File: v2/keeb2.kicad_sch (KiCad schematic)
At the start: 24 parts, among them J1 AVR-ISP-6, J3 AudioJack4, SW2 SW_Push_Reset, SW71 RotaryEncoder_Switch, U1 ATmega32U4-A, Y1 XTAL

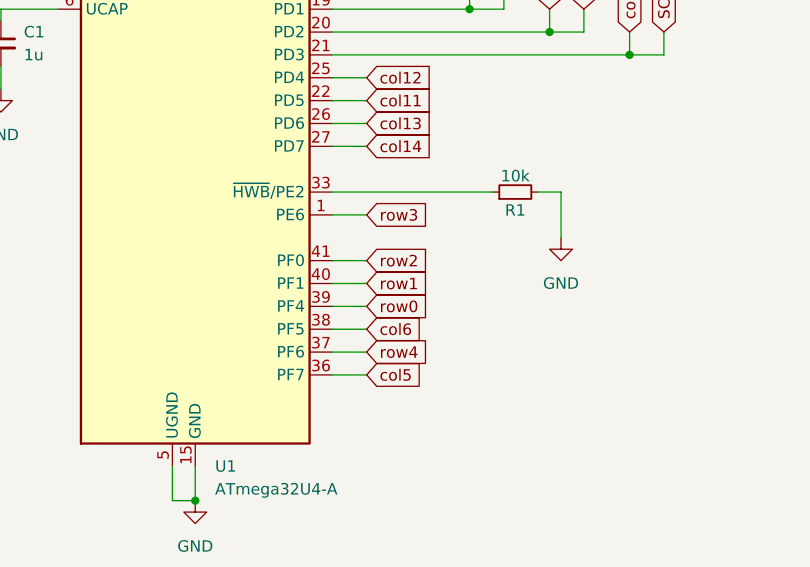
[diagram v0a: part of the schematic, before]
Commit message: Linked part of the design; need to move reset button &  ISP
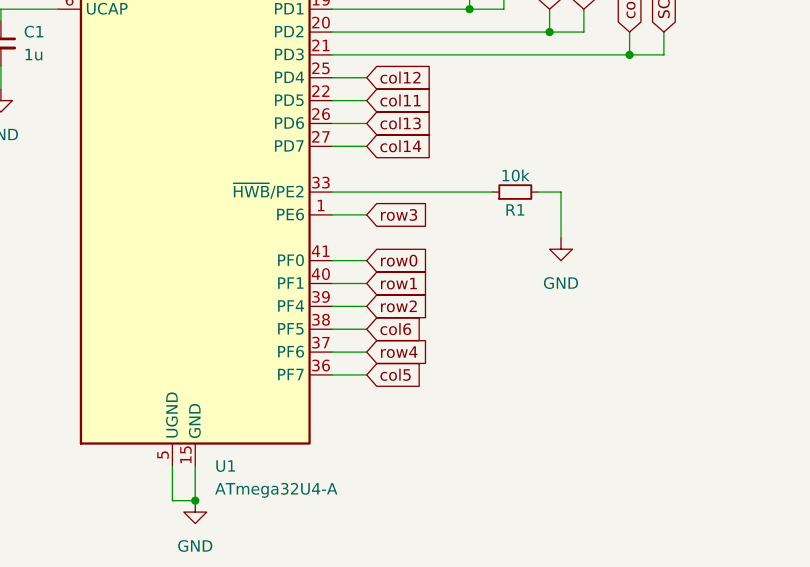
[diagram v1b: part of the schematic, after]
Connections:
- net row0: now also U1.41 (PF0); no longer U1.39 (PF4)
- net row2: now also U1.39 (PF4); no longer U1.41 (PF0)

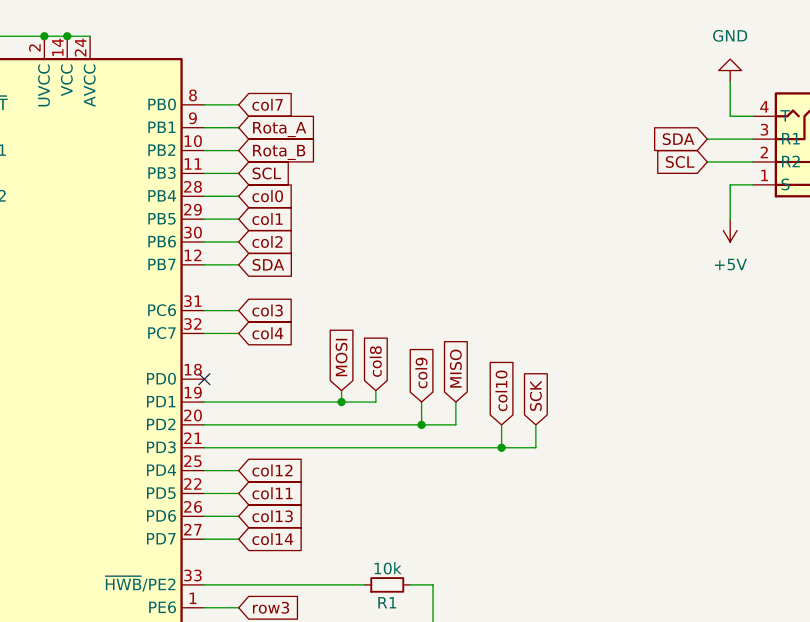
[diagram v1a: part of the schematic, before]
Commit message: Moved ISP and reset button. Finished routing
Moved the ISP IO to make it easier to route them to the MCU
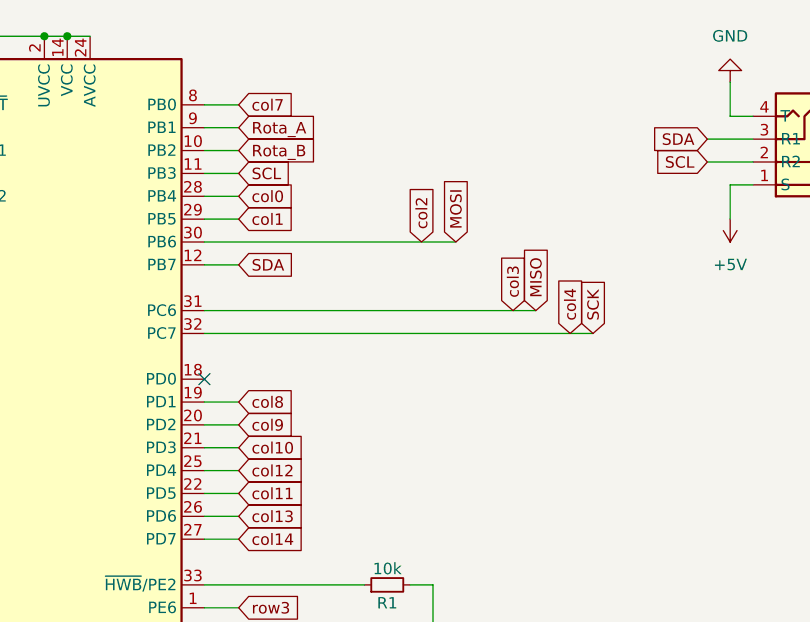
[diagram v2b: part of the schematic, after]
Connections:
- net col2 is gone; now on net MOSI: U1.30 (PB6)
- net col3 is gone; now on net MISO: U1.31 (PC6)
- net col4 is gone; now on net SCK: U1.32 (PC7)
- net MISO: no longer U1.20 (PD2)
- net MOSI: no longer U1.19 (PD1)
- net SCK: no longer U1.21 (PD3)
- new net col10: U1.21 (PD3)
- new net col8: U1.19 (PD1)
- new net col9: U1.20 (PD2)
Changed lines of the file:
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@@
-	)
-	(junction
-		(at 243.84 85.09)
-		(diameter 0)
-		(color 0 0 0 0)
-	)
-	(junction
-		(at 234.95 82.55)
-		(diameter 0)
-		(color 0 0 0 0)
 	)
 	(junction
@@
 	)
 	(junction
-		(at 226.06 80.01)
-		(diameter 0)
-		(color 0 0 0 0)
-	)
-	(junction
 		(at 66.04 93.98)
 		(diameter 0)
@@
 	(wire
 		(pts
-			(xy 210.82 72.39) (xy 214.63 72.39)
+			(xy 210.82 72.39) (xy 254 72.39)
 		)
 		(stroke
@@
 	(wire
 		(pts
-			(xy 234.95 82.55) (xy 238.76 82.55)
-		)
-		(stroke
-			(width 0)
-			(type default)
-		)
-	)
-	(wire
-		(pts
 			(xy 128.27 52.07) (xy 134.62 52.07)
 		)
@@
 	(wire
 		(pts
-			(xy 210.82 80.01) (xy 226.06 80.01)
-		)
-		(stroke
-			(width 0)
-			(type default)
-		)
-	)
-	(wire
-		(pts
 			(xy 173.99 80.01) (xy 173.99 81.28)
 		)
@@
 	(wire
 		(pts
-			(xy 243.84 85.09) (xy 247.65 85.09)
-		)
-		(stroke
-			(width 0)
-			(type default)
-		)
-	)
-	(wire
-		(pts
 			(xy 210.82 115.57) (xy 214.63 115.57)
 		)
@@
 	(wire
 		(pts
-			(xy 210.82 62.23) (xy 214.63 62.23)
-		)
-		(stroke
-			(width 0)
-			(type default)
-		)
-	)
-	(wire
-		(pts
-			(xy 247.65 82.55) (xy 247.65 85.09)
+			(xy 210.82 62.23) (xy 238.76 62.23)
 		)
 		(stroke
@@
 	(wire
 		(pts
+			(xy 210.82 85.09) (xy 214.63 85.09)
+		)
+		(stroke
+			(width 0)
+			(type default)
+		)
+	)
+	(wire
+		(pts
 			(xy 210.82 54.61) (xy 214.63 54.61)
 		)
@@
 	(wire
 		(pts
-			(xy 210.82 85.09) (xy 243.84 85.09)
-		)
-		(stroke
-			(width 0)
-			(type default)
-		)
-	)
-	(wire
-		(pts
 			(xy 50.8 33.02) (xy 50.8 38.1)
 		)
@@
 	(wire
 		(pts
-			(xy 210.82 82.55) (xy 234.95 82.55)
-		)
-		(stroke
-			(width 0)
-			(type default)
-		)
-	)
-	(wire
-		(pts
 			(xy 210.82 46.99) (xy 214.63 46.99)
 		)
@@
 	(wire
 		(pts
-			(xy 226.06 80.01) (xy 229.87 80.01)
-		)
-		(stroke
-			(width 0)
-			(type default)
-		)
-	)
-	(wire
-		(pts
 			(xy 210.82 90.17) (xy 214.63 90.17)
 		)
@@
 	(wire
 		(pts
+			(xy 210.82 80.01) (xy 214.63 80.01)
+		)
+		(stroke
+			(width 0)
+			(type default)
+		)
+	)
+	(wire
+		(pts
 			(xy 45.72 78.74) (xy 45.72 83.82)
 		)
@@
 	(wire
 		(pts
+			(xy 210.82 82.55) (xy 214.63 82.55)
+		)
+		(stroke
+			(width 0)
+			(type default)
+		)
+	)
+	(wire
+		(pts
 			(xy 39.37 76.2) (xy 46.99 76.2)
 		)
@@
 	(wire
 		(pts
-			(xy 210.82 69.85) (xy 214.63 69.85)
+			(xy 210.82 69.85) (xy 247.65 69.85)
 		)
 		(stroke
@@
 	(wire
 		(pts
-			(xy 234.95 82.55) (xy 234.95 80.01)
-		)
-		(stroke
-			(width 0)
-			(type default)
-		)
-	)
-	(wire
-		(pts
 			(xy 62.23 83.82) (xy 63.5 83.82)
 		)
@@
 	(wire
 		(pts
-			(xy 226.06 80.01) (xy 226.06 78.74)
-		)
-		(stroke
-			(width 0)
-			(type default)
-		)
-	)
-	(wire
-		(pts
 			(xy 269.24 55.88) (xy 269.24 59.69)
 		)
@@
 	(wire
 		(pts
-			(xy 238.76 80.01) (xy 238.76 82.55)
-		)
-		(stroke
-			(width 0)
-			(type default)
-		)
-	)
-	(wire
-		(pts
 			(xy 123.19 157.48) (xy 128.27 157.48)
 		)
@@
 	(wire
 		(pts
-			(xy 229.87 78.74) (xy 229.87 80.01)
-		)
-		(stroke
-			(width 0)
-			(type default)
-		)
-	)
-	(wire
-		(pts
 			(xy 39.37 33.02) (xy 39.37 38.1)
 		)
@@
 		(pts
 			(xy 62.23 27.94) (xy 62.23 22.86)
-		)
-		(stroke
-			(width 0)
-			(type default)
-		)
-	)
-	(wire
-		(pts
-			(xy 243.84 85.09) (xy 243.84 82.55)
 		)
 		(stroke
@@
 	(global_label "col2"
 		(shape input)
-		(at 214.63 62.23 0)
-		(fields_autoplaced yes)
-		(effects
-			(font
-				(size 1.27 1.27)
-			)
-			(justify left)
-		)
-		(property "Intersheetrefs" "${INTERSHEET_REFS}"
-			(at 221.7275 62.23 0)
+		(at 234.95 62.23 90)
+		(fields_autoplaced yes)
+		(effects
+			(font
+				(size 1.27 1.27)
+			)
+			(justify left)
+		)
+		(property "Intersheetrefs" "${INTERSHEET_REFS}"
+			(at 234.95 55.1325 90)
 			(effects
 				(font
@@
 	(global_label "col9"
 		(shape input)
-		(at 234.95 80.01 90)
-		(fields_autoplaced yes)
-		(effects
-			(font
-				(size 1.27 1.27)
-			)
-			(justify left)
-		)
-		(property "Intersheetrefs" "${INTERSHEET_REFS}"
-			(at 234.95 72.9125 90)
+		(at 214.63 82.55 0)
+		(fields_autoplaced yes)
+		(effects
+			(font
+				(size 1.27 1.27)
+			)
+			(justify left)
+		)
+		(property "Intersheetrefs" "${INTERSHEET_REFS}"
+			(at 221.7275 82.55 0)
 			(effects
 				(font
@@
 	(global_label "MISO"
 		(shape input)
-		(at 238.76 80.01 90)
-		(fields_autoplaced yes)
-		(effects
-			(font
-				(size 1.27 1.27)
-			)
-			(justify left)
-		)
-		(property "Intersheetrefs" "${INTERSHEET_REFS}"
-			(at 238.76 72.4286 90)
+		(at 247.65 69.85 90)
+		(fields_autoplaced yes)
+		(effects
+			(font
+				(size 1.27 1.27)
+			)
+			(justify left)
+		)
+		(property "Intersheetrefs" "${INTERSHEET_REFS}"
+			(at 247.65 62.2686 90)
 			(effects
 				(font
@@
 	(global_label "MOSI"
 		(shape input)
-		(at 226.06 78.74 90)
-		(fields_autoplaced yes)
-		(effects
-			(font
-				(size 1.27 1.27)
-			)
-			(justify left)
-		)
-		(property "Intersheetrefs" "${INTERSHEET_REFS}"
-			(at 226.06 71.1586 90)
+		(at 238.76 62.23 90)
+		(fields_autoplaced yes)
+		(effects
+			(font
+				(size 1.27 1.27)
+			)
+			(justify left)
+		)
+		(property "Intersheetrefs" "${INTERSHEET_REFS}"
+			(at 238.76 54.6486 90)
 			(effects
 				(font
@@
 	(global_label "SCK"
 		(shape input)
-		(at 247.65 82.55 90)
-		(fields_autoplaced yes)
-		(effects
-			(font
-				(size 1.27 1.27)
-			)
-			(justify left)
-		)
-		(property "Intersheetrefs" "${INTERSHEET_REFS}"
-			(at 247.65 75.8153 90)
+		(at 254 72.39 90)
+		(fields_autoplaced yes)
+		(effects
+			(font
+				(size 1.27 1.27)
+			)
+			(justify left)
+		)
+		(property "Intersheetrefs" "${INTERSHEET_REFS}"
+			(at 254 65.6553 90)
 			(effects
 				(font
@@
 	(global_label "col3"
 		(shape input)
-		(at 214.63 69.85 0)
-		(fields_autoplaced yes)
-		(effects
-			(font
-				(size 1.27 1.27)
-			)
-			(justify left)
-		)
-		(property "Intersheetrefs" "${INTERSHEET_REFS}"
-			(at 221.7275 69.85 0)
+		(at 245.11 69.85 90)
+		(fields_autoplaced yes)
+		(effects
+			(font
+				(size 1.27 1.27)
+			)
+			(justify left)
+		)
+		(property "Intersheetrefs" "${INTERSHEET_REFS}"
+			(at 245.11 62.7525 90)
 			(effects
 				(font
@@
 	(global_label "col10"
 		(shape input)
-		(at 243.84 82.55 90)
-		(fields_autoplaced yes)
-		(effects
-			(font
-				(size 1.27 1.27)
-			)
-			(justify left)
-		)
-		(property "Intersheetrefs" "${INTERSHEET_REFS}"
-			(at 243.84 74.243 90)
+		(at 214.63 85.09 0)
+		(fields_autoplaced yes)
+		(effects
+			(font
+				(size 1.27 1.27)
+			)
+			(justify left)
+		)
+		(property "Intersheetrefs" "${INTERSHEET_REFS}"
+			(at 222.937 85.09 0)
 			(effects
 				(font
@@
 	(global_label "col4"
 		(shape input)
-		(at 214.63 72.39 0)
-		(fields_autoplaced yes)
-		(effects
-			(font
-				(size 1.27 1.27)
-			)
-			(justify left)
-		)
-		(property "Intersheetrefs" "${INTERSHEET_REFS}"
-			(at 221.7275 72.39 0)
+		(at 251.46 72.39 90)
+		(fields_autoplaced yes)
+		(effects
+			(font
+				(size 1.27 1.27)
+			)
+			(justify left)
+		)
+		(property "Intersheetrefs" "${INTERSHEET_REFS}"
+			(at 251.46 65.2925 90)
 			(effects
 				(font
@@
 	(global_label "col8"
 		(shape input)
-		(at 229.87 78.74 90)
-		(fields_autoplaced yes)
-		(effects
-			(font
-				(size 1.27 1.27)
-			)
-			(justify left)
-		)
-		(property "Intersheetrefs" "${INTERSHEET_REFS}"
-			(at 229.87 71.6425 90)
-			(effects
-				(font
+		(at 214.63 80.01 0)
+		(fields_autoplaced yes)
+		(effects
+			(font
+				(size 1.27 1.27)
+			)
+			(justify left)
+		)
+		(property "Intersheetrefs" "${INTERSHEET_REFS}"
+			(at 221.7275 80.01 0)
+			(effects
+				(font

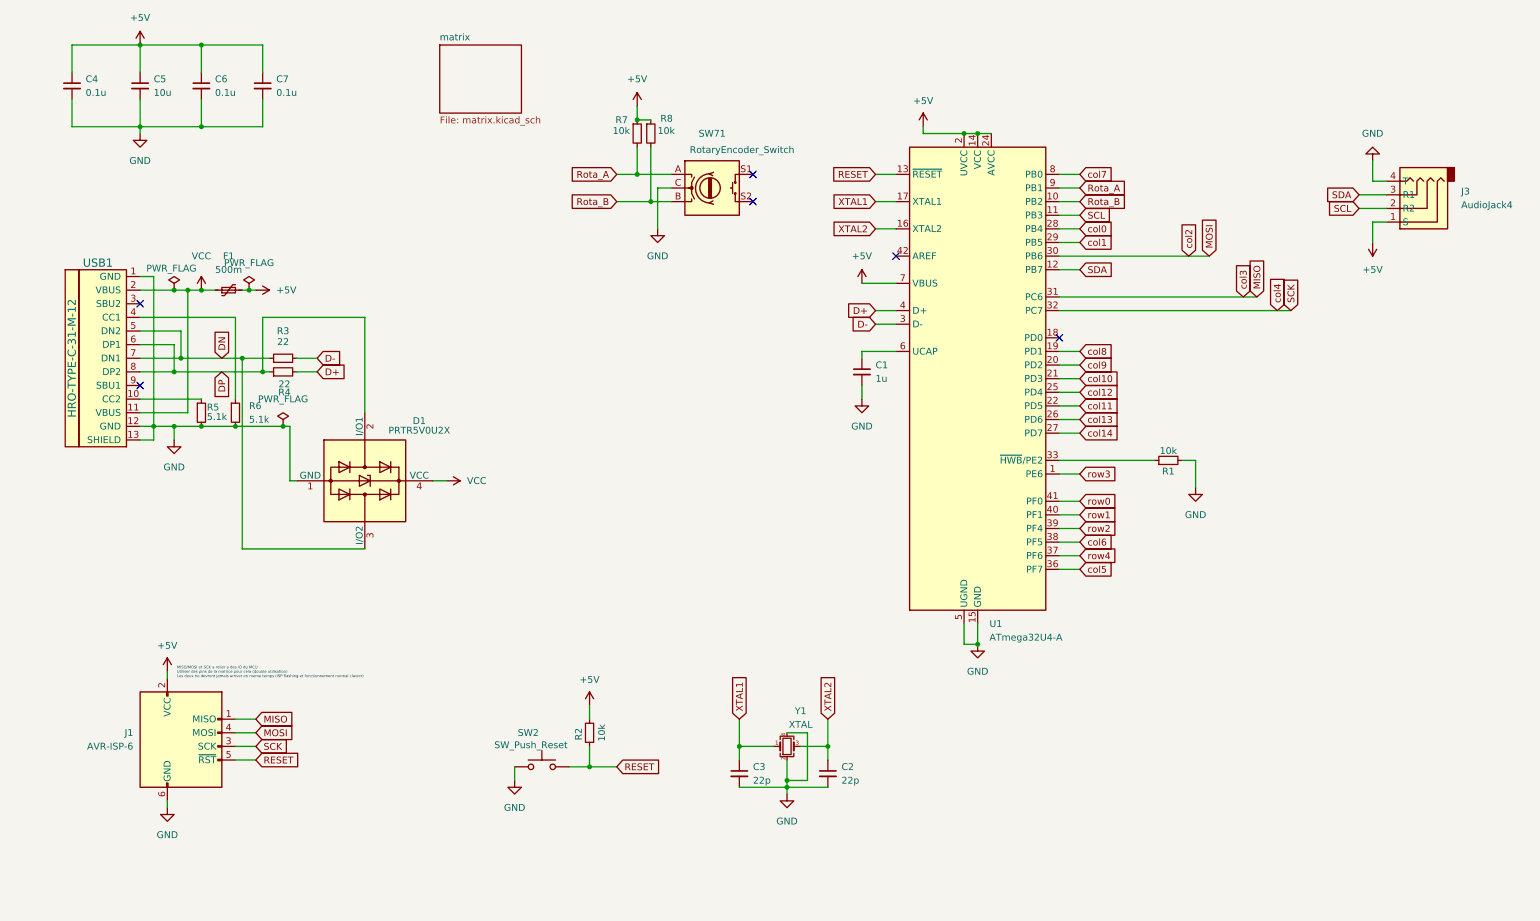
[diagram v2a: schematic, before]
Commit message: Change outline to fit new case
Add mounting holes at correct location

case height : 96 mm
pcb height : 95.5mm

case length : 305 mm
pcb length : 304.5 mm
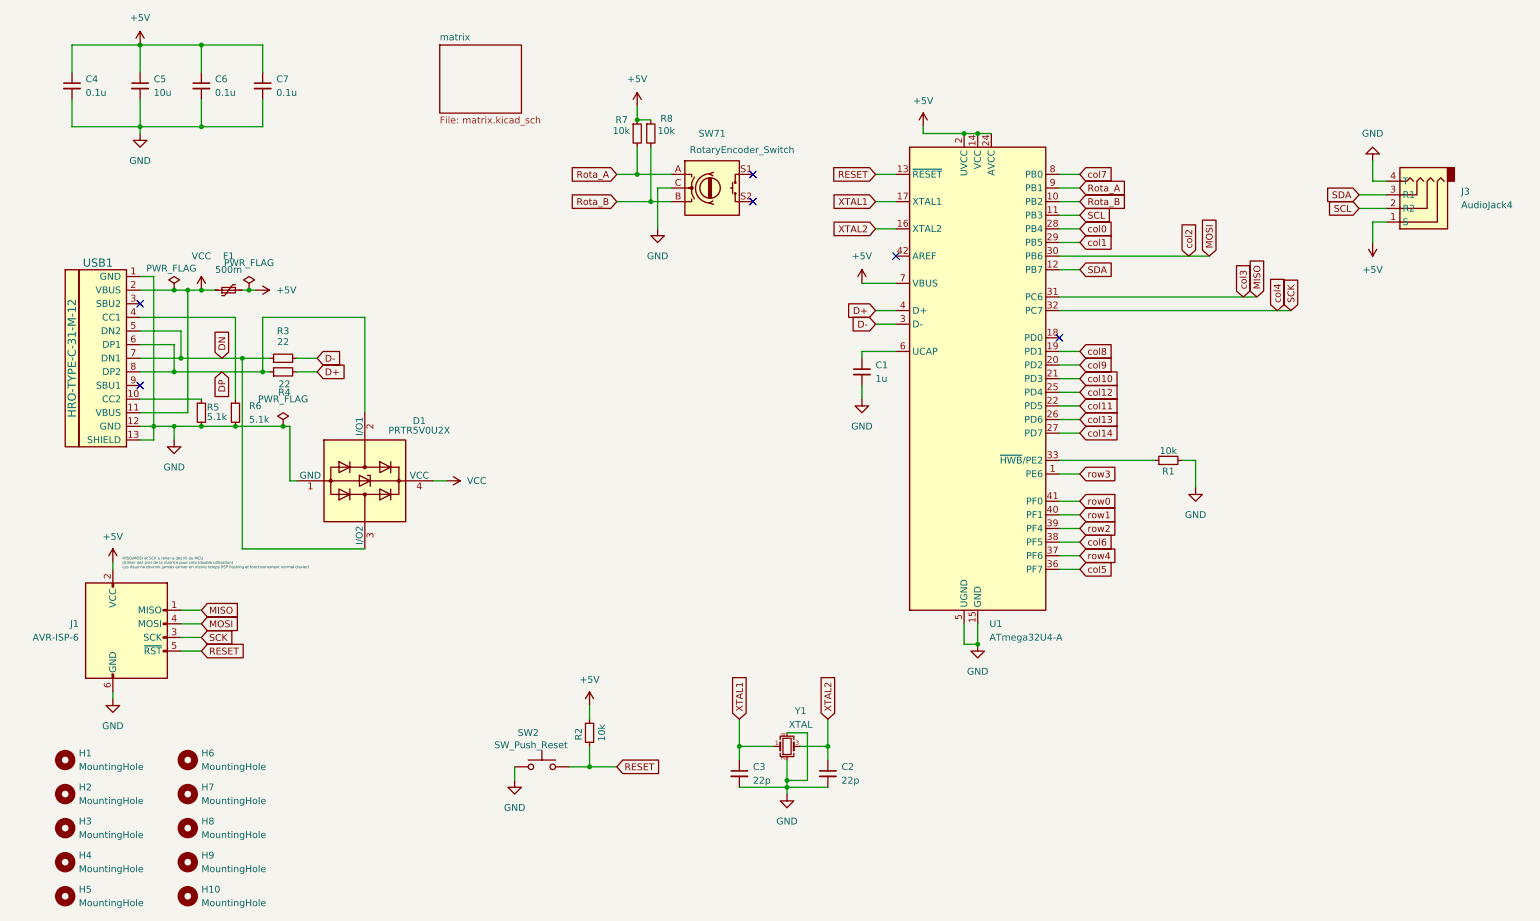
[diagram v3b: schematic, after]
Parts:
- added H1, H10, H2, H3, H4, H5, H6, H7, H8, H9: MountingHole, MountingHole:MountingHole_2.1mm, symbol Mechanical:MountingHole
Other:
- moved on the sheet: J1
